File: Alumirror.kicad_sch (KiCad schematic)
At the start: 42 parts, among them J1 USB_C_Receptacle_USB2.0_16P_2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, J2 USB_C_Receptacle_USB2.0_16P_2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, J3 USB_C_Receptacle_USB2.0_16P_2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, J4 USB_C_Receptacle_USB2.0_16P_2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, SW1 BOOT, U1 CH552T, U2 CH552T, U3 USBLC6-2P6, U4 USBLC6-2P6, U5 USBLC6-2P6, U6 USBLC6-2P6

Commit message: Switch R14 back to 2010 size
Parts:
- R14: footprint Resistor_SMD:R_0805_2012Metric -> Resistor_SMD:R_2010_5025Metric
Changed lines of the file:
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@@
 			)
 		)
-		(property "Footprint" "Resistor_SMD:R_0805_2012Metric"
+		(property "Footprint" "Resistor_SMD:R_2010_5025Metric"
 			(at 128.27 62.738 90)
 			(effects

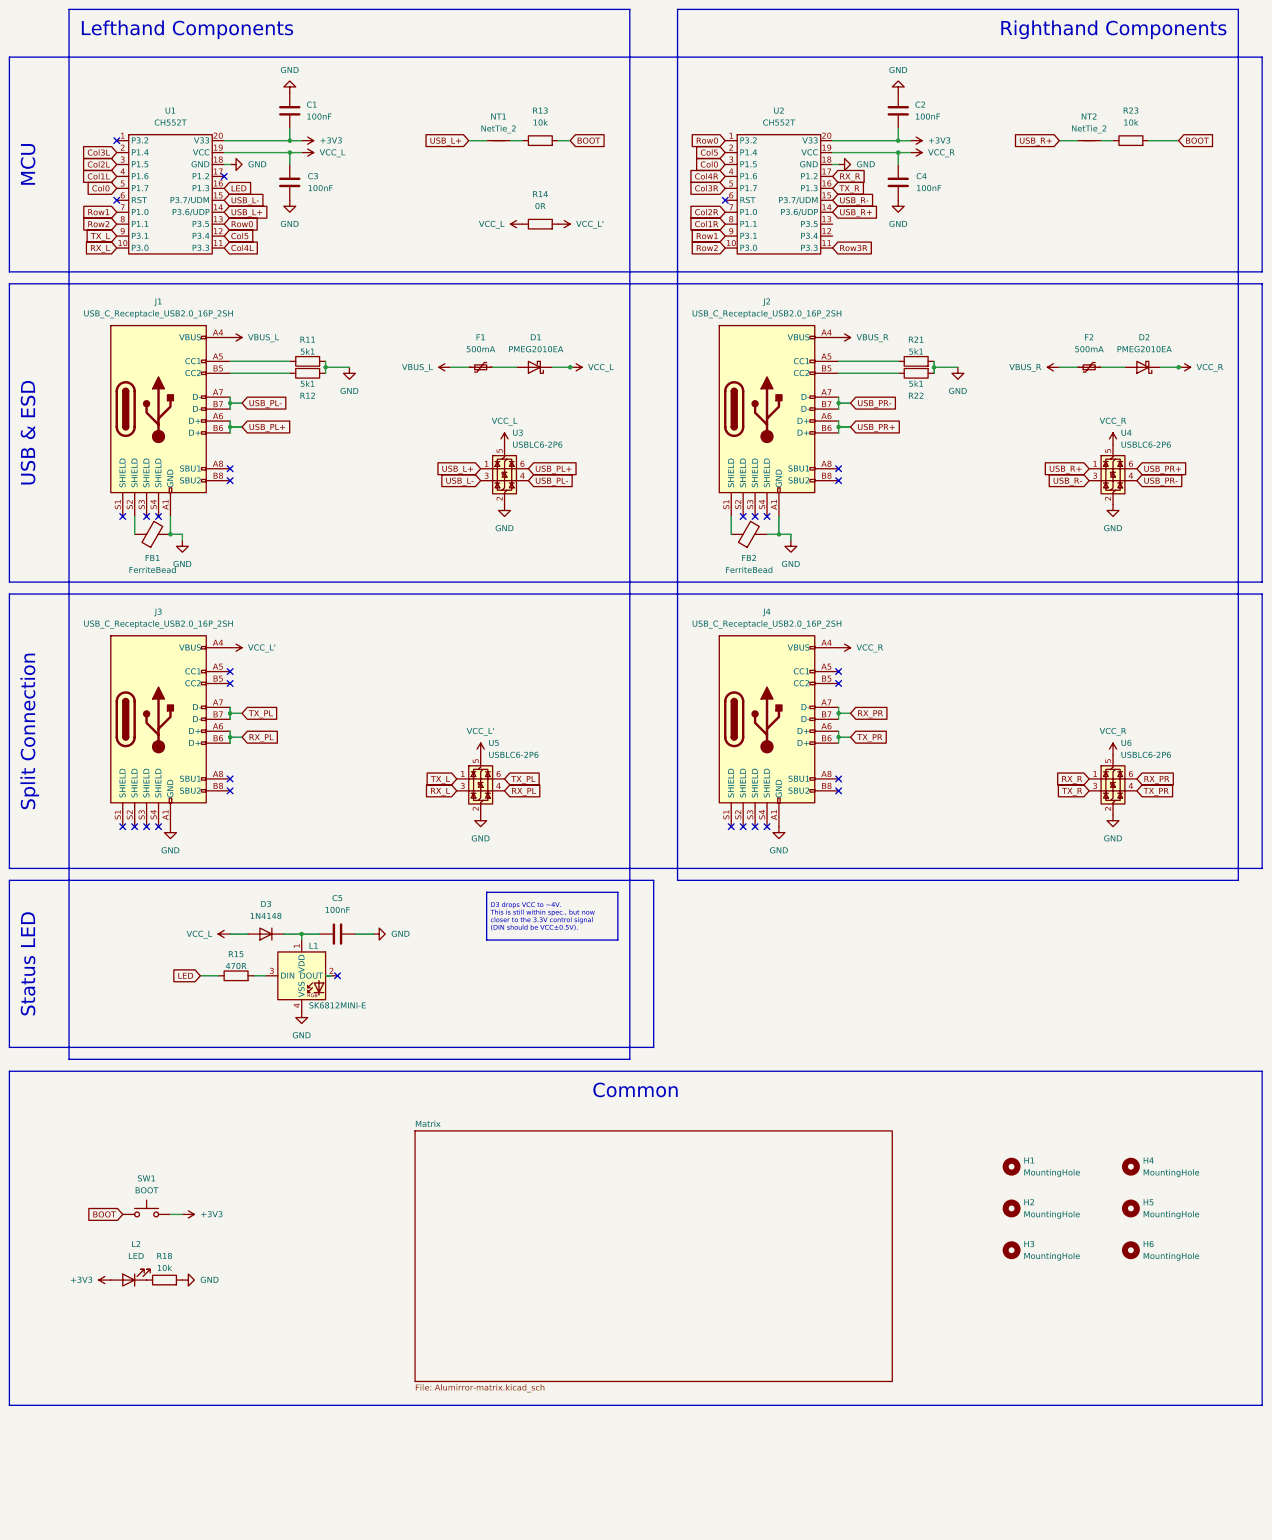
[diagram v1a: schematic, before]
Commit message: Shuffle components around again and fix DRC messages
 * Move split connection ESD chip to inside of associated USB port instead of above.
 * Scootch MCUs down.
 * Reduce clearance of ESD chip ground pin polygon pad.
 * Change solder nut hole to through-hole pad instead of NPT hole and solid pad.
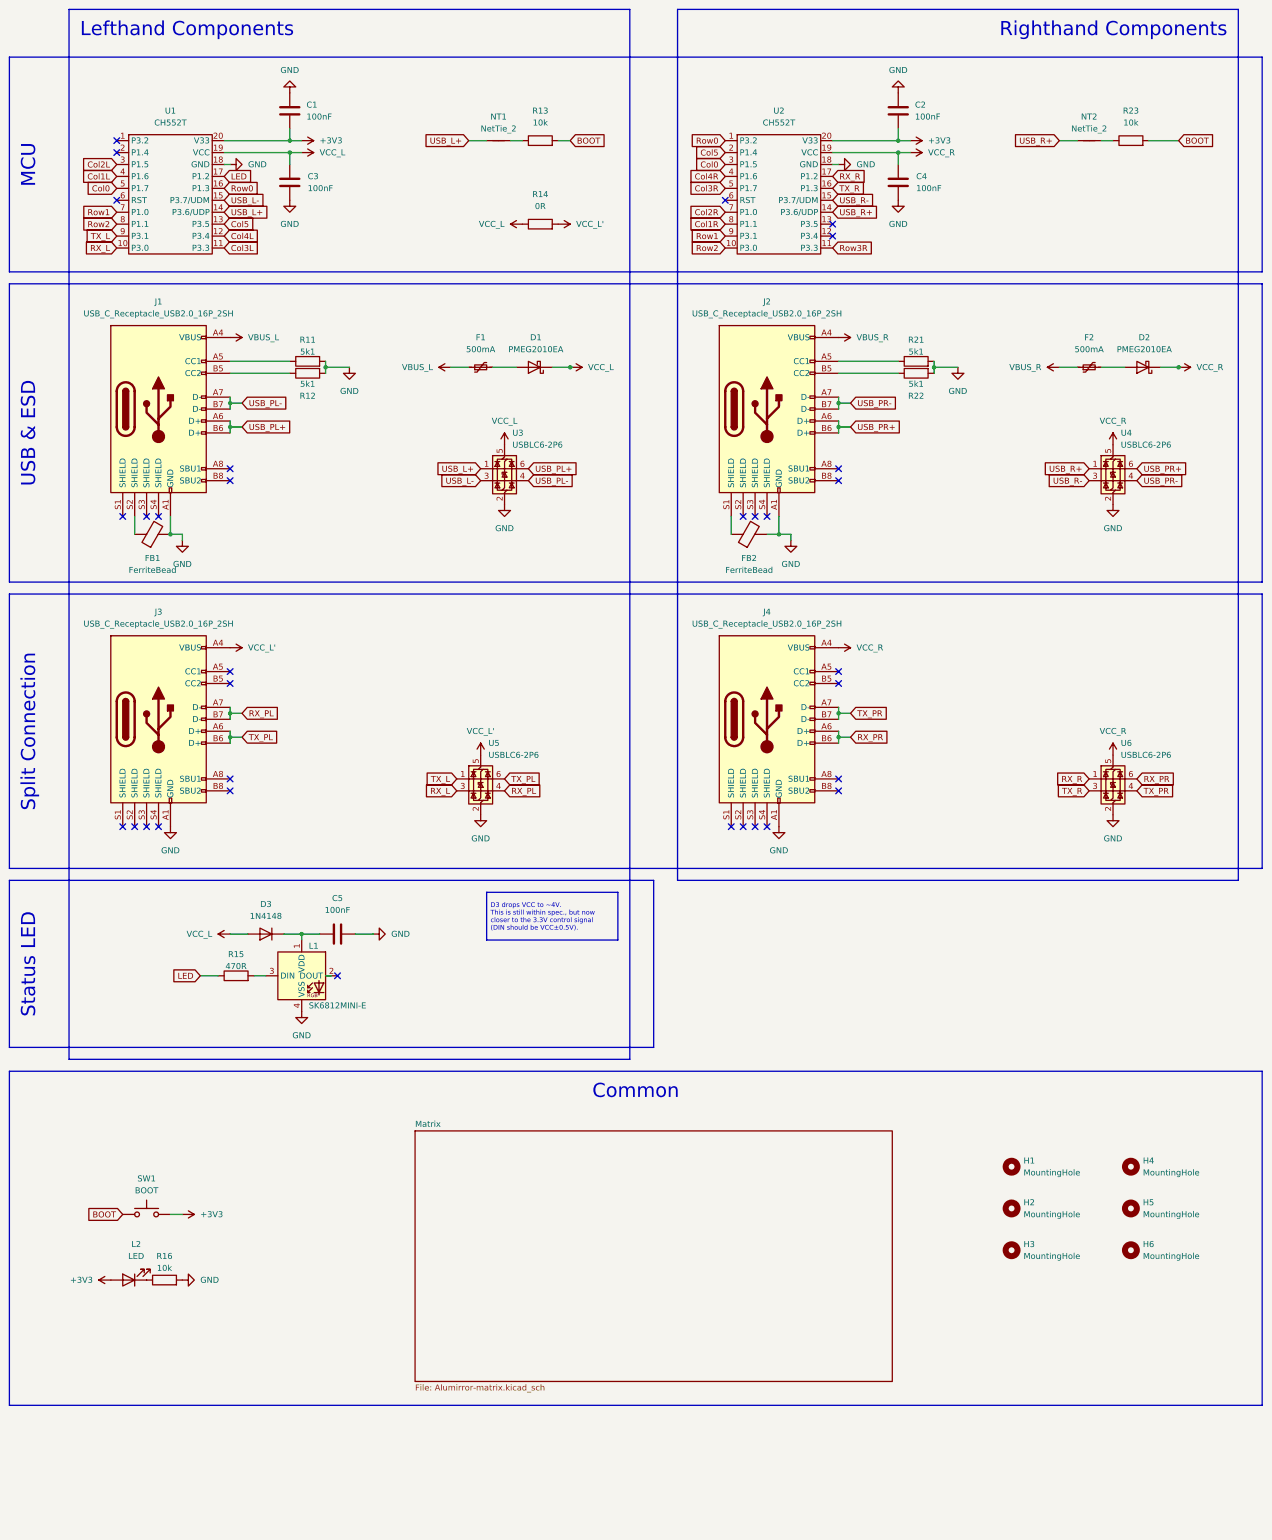
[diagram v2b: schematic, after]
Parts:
- renumbered R18 to R16
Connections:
- net Col3L: now also U1.11 (P3.3); no longer U1.2 (P1.4)
- net Col4L: now also U1.12 (P3.4); no longer U1.11 (P3.3)
- net Col5: now also U1.13 (P3.5); no longer U1.12 (P3.4)
- net LED: now also U1.17 (P1.2); no longer U1.16 (P1.3)
- net RX_PL: now also J3.A7 (D-), J3.B7 (D-); no longer J3.A6 (D+), J3.B6 (D+)
- net RX_PR: now also J4.A6 (D+), J4.B6 (D+); no longer J4.A7 (D-), J4.B7 (D-)
- net Row0: now also U1.16 (P1.3); no longer U1.13 (P3.5)
- net TX_PL: now also J3.A6 (D+), J3.B6 (D+); no longer J3.A7 (D-), J3.B7 (D-)
- net TX_PR: now also J4.A7 (D-), J4.B7 (D-); no longer J4.A6 (D+), J4.B6 (D+)
- no-connect marks 31 -> 33
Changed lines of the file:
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@@
 	)
 	(no_connect
+		(at 190.5 60.96)
+	)
+	(no_connect
 		(at 173.99 189.23)
 	)
@@
 	)
 	(no_connect
+		(at 190.5 63.5)
+	)
+	(no_connect
 		(at 85.09 220.98)
 	)
@@
 	)
 	(no_connect
-		(at 60.96 50.8)
+		(at 38.1 45.72)
 	)
 	(no_connect
@@
 	(global_label "Col4L"
 		(shape input)
-		(at 60.96 66.04 0)
+		(at 60.96 63.5 0)
 		(fields_autoplaced yes)
 		(effects
@@
 		)
 		(property "Intersheetrefs" "${INTERSHEET_REFS}"
-			(at 69.267 66.04 0)
+			(at 69.267 63.5 0)
 			(effects
 				(font
@@
 	(global_label "LED"
 		(shape input)
-		(at 60.96 53.34 0)
+		(at 60.96 50.8 0)
 		(fields_autoplaced yes)
 		(effects
@@
 		)
 		(property "Intersheetrefs" "${INTERSHEET_REFS}"
-			(at 67.3923 53.34 0)
+			(at 67.3923 50.8 0)
 			(effects
 				(font
@@
 	(global_label "RX_PL"
 		(shape input)
-		(at 64.77 170.18 0)
+		(at 64.77 165.1 0)
 		(fields_autoplaced yes)
 		(effects
@@
 		)
 		(property "Intersheetrefs" "${INTERSHEET_REFS}"
-			(at 73.5004 170.18 0)
+			(at 73.5004 165.1 0)
 			(effects
 				(font
@@
 	(global_label "Col3L"
 		(shape input)
-		(at 38.1 45.72 180)
+		(at 60.96 66.04 0)
 		(fields_autoplaced yes)
 		(effects
@@
 				(size 1.27 1.27)
 			)
-			(justify right)
+			(justify left)
 		)
 		(property "Intersheetrefs" "${INTERSHEET_REFS}"
-			(at 29.793 45.72 0)
+			(at 69.267 66.04 0)
 			(effects
 				(font
 					(size 1.27 1.27)
 				)
-				(justify right)
+				(justify left)
 				(hide yes)
 			)
@@
 	(global_label "Col5"
 		(shape input)
-		(at 60.96 63.5 0)
+		(at 60.96 60.96 0)
 		(fields_autoplaced yes)
 		(effects
@@
 		)
 		(property "Intersheetrefs" "${INTERSHEET_REFS}"
-			(at 68.2389 63.5 0)
+			(at 68.2389 60.96 0)
 			(effects
 				(font
@@
 	(global_label "TX_PL"
 		(shape input)
-		(at 64.77 165.1 0)
+		(at 64.77 170.18 0)
 		(fields_autoplaced yes)
 		(effects
@@
 		)
 		(property "Intersheetrefs" "${INTERSHEET_REFS}"
-			(at 73.198 165.1 0)
+			(at 73.198 170.18 0)
 			(effects
 				(font
@@
 	(global_label "RX_PR"
 		(shape input)
-		(at 194.31 165.1 0)
+		(at 194.31 170.18 0)
 		(fields_autoplaced yes)
 		(effects
@@
 		)
 		(property "Intersheetrefs" "${INTERSHEET_REFS}"
-			(at 203.2823 165.1 0)
+			(at 203.2823 170.18 0)
 			(effects
 				(font
@@
 	(global_label "TX_PR"
 		(shape input)
-		(at 194.31 170.18 0)
+		(at 194.31 165.1 0)
 		(fields_autoplaced yes)
 		(effects
@@
 		)
 		(property "Intersheetrefs" "${INTERSHEET_REFS}"
-			(at 202.9799 170.18 0)
+			(at 202.9799 165.1 0)
 			(effects
 				(font
@@
 	(global_label "Row0"
 		(shape input)
-		(at 60.96 60.96 0)
+		(at 60.96 53.34 0)
 		(fields_autoplaced yes)
 		(effects
@@
 		)
 		(property "Intersheetrefs" "${INTERSHEET_REFS}"
-			(at 68.9042 60.96 0)
+			(at 68.9042 53.34 0)
 			(effects
 				(font
@@
 		(on_board yes)
 		(dnp no)
-		(property "Reference" "R18"
+		(property "Reference" "R16"
 			(at 48.26 280.67 90)
 			(effects
@@
 			(project "Alumirror"
 				(path "/52f043ac-ccff-4c85-bc10-2db9d3c9e3f3"
-					(reference "R18")
+					(reference "R16")
 					(unit 1)
 				)

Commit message: Renumber components
 * For single-digit components:
   * Odd numbers are populated on the lefthand board only
   * Even numbers are populated on the righthand board only
 * Double-digit components are populated on both sides
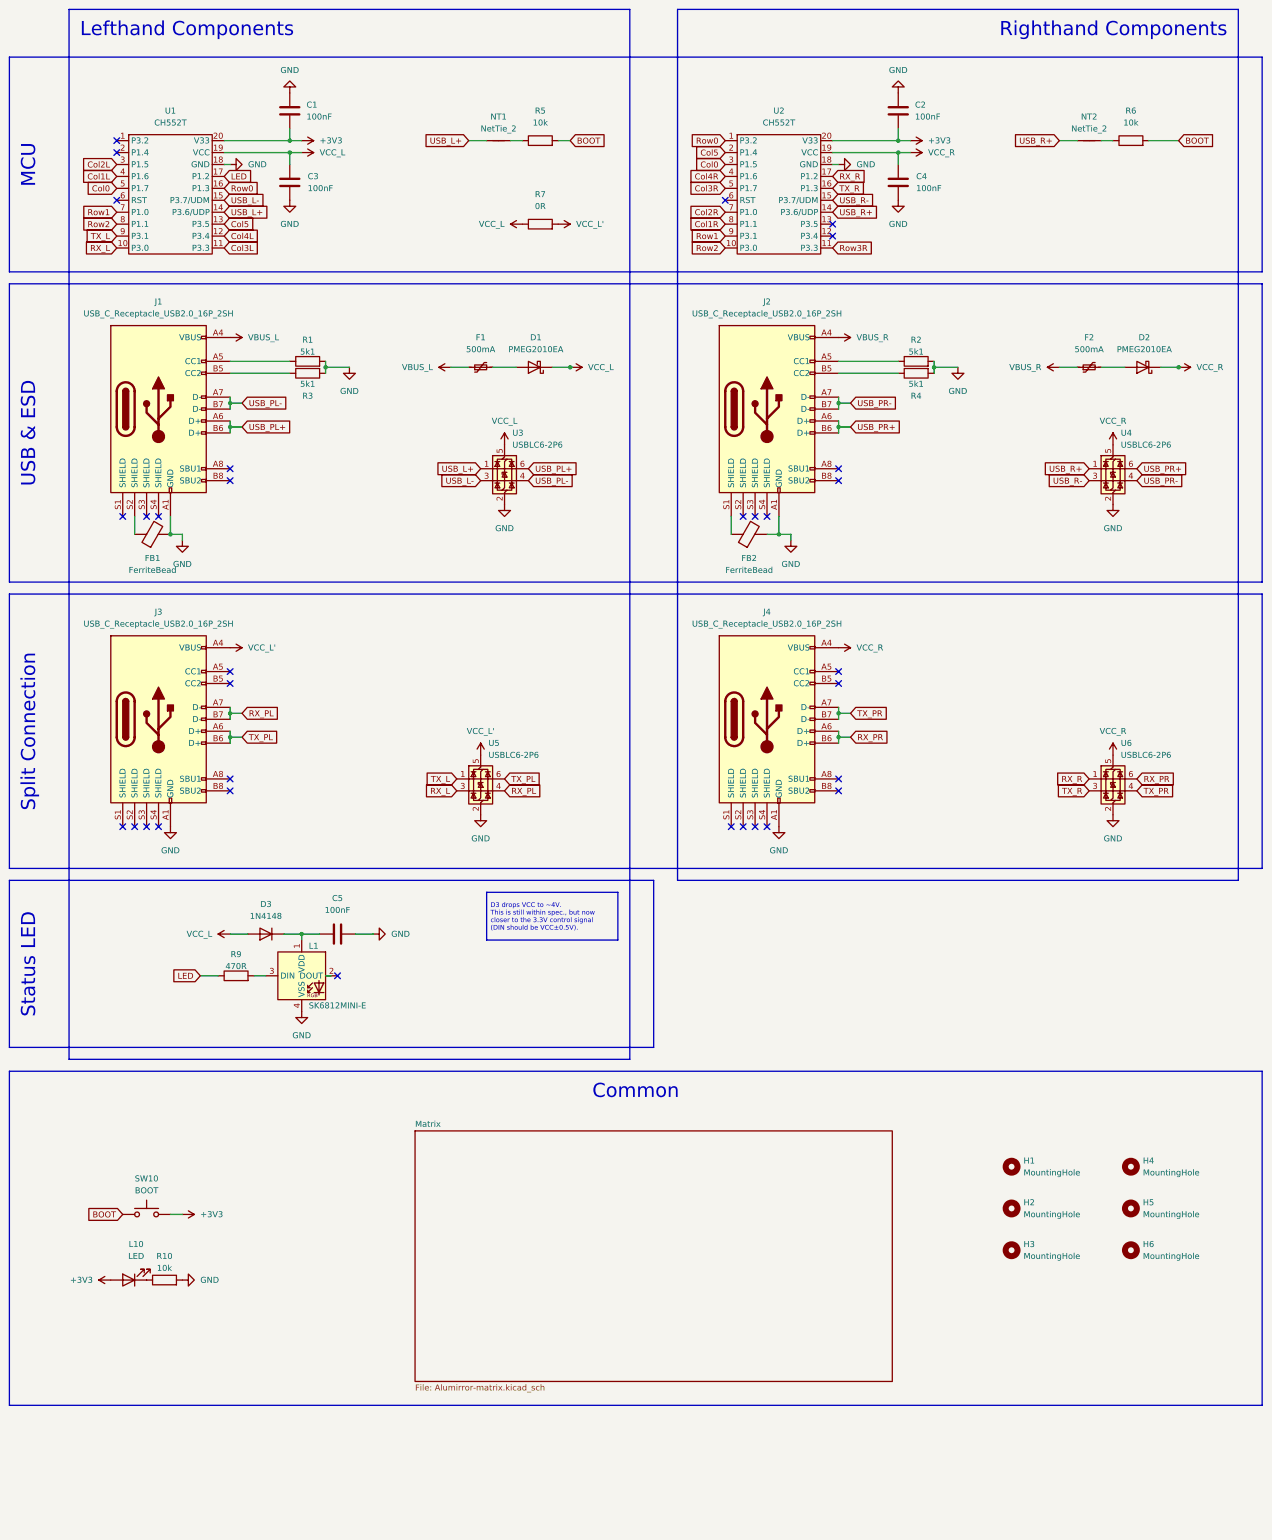
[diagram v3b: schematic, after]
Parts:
- renumbered L2 to L10, R11 to R1, R16 to R10, R21 to R2, R12 to R3, R22 to R4, R13 to R5, R23 to R6, R14 to R7, R15 to R9, SW1 to SW10
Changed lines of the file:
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@@
 		(dnp no)
 		(fields_autoplaced yes)
-		(property "Reference" "L2"
+		(property "Reference" "L10"
 			(at 42.2275 278.13 0)
 			(effects
@@
 			(project ""
 				(path "/52f043ac-ccff-4c85-bc10-2db9d3c9e3f3"
-					(reference "L2")
+					(reference "L10")
 					(unit 1)
 				)
@@
 		(on_board yes)
 		(dnp no)
-		(property "Reference" "R21"
+		(property "Reference" "R2"
 			(at 208.28 85.598 90)
 			(effects
@@
 			(project "Alumirror"
 				(path "/52f043ac-ccff-4c85-bc10-2db9d3c9e3f3"
-					(reference "R21")
+					(reference "R2")
 					(unit 1)
 				)
@@
 		(on_board yes)
 		(dnp no)
-		(property "Reference" "R11"
+		(property "Reference" "R1"
 			(at 78.74 85.598 90)
 			(effects
@@
 			(project "Alumirror"
 				(path "/52f043ac-ccff-4c85-bc10-2db9d3c9e3f3"
-					(reference "R11")
+					(reference "R1")
 					(unit 1)
 				)
@@
 		(dnp no)
 		(fields_autoplaced yes)
-		(property "Reference" "R13"
+		(property "Reference" "R5"
 			(at 128.27 36.83 90)
 			(effects
@@
 			(project "Alumirror"
 				(path "/52f043ac-ccff-4c85-bc10-2db9d3c9e3f3"
-					(reference "R13")
+					(reference "R5")
 					(unit 1)
 				)
@@
 		(on_board yes)
 		(dnp no)
-		(property "Reference" "R22"
+		(property "Reference" "R4"
 			(at 208.28 97.536 90)
 			(effects
@@
 			(project "Alumirror"
 				(path "/52f043ac-ccff-4c85-bc10-2db9d3c9e3f3"
-					(reference "R22")
+					(reference "R4")
 					(unit 1)
 				)
@@
 		(on_board yes)
 		(dnp no)
-		(property "Reference" "R15"
+		(property "Reference" "R9"
 			(at 63.5 216.408 90)
 			(effects
@@
 			(project "Alumirror"
 				(path "/52f043ac-ccff-4c85-bc10-2db9d3c9e3f3"
-					(reference "R15")
+					(reference "R9")
 					(unit 1)
 				)
@@
 		(dnp no)
 		(fields_autoplaced yes)
-		(property "Reference" "R23"
+		(property "Reference" "R6"
 			(at 254 36.83 90)
 			(effects
@@
 			(project "Alumirror"
 				(path "/52f043ac-ccff-4c85-bc10-2db9d3c9e3f3"
-					(reference "R23")
+					(reference "R6")
 					(unit 1)
 				)
@@
 		(on_board yes)
 		(dnp no)
-		(property "Reference" "R16"
+		(property "Reference" "R10"
 			(at 48.26 280.67 90)
 			(effects
@@
 			(project "Alumirror"
 				(path "/52f043ac-ccff-4c85-bc10-2db9d3c9e3f3"
-					(reference "R16")
+					(reference "R10")
 					(unit 1)
 				)
@@
 		(on_board yes)
 		(dnp no)
-		(property "Reference" "R12"
+		(property "Reference" "R3"
 			(at 78.74 97.536 90)
 			(effects
@@
 			(project "Alumirror"
 				(path "/52f043ac-ccff-4c85-bc10-2db9d3c9e3f3"
-					(reference "R12")
+					(reference "R3")
 					(unit 1)
 				)
@@
 		(dnp no)
 		(fields_autoplaced yes)
-		(property "Reference" "R14"
+		(property "Reference" "R7"
 			(at 128.27 54.61 90)
 			(effects
@@
 			(project "Alumirror"
 				(path "/52f043ac-ccff-4c85-bc10-2db9d3c9e3f3"
-					(reference "R14")
+					(reference "R7")
 					(unit 1)
 				)
@@
 		(dnp no)
 		(fields_autoplaced yes)
-		(property "Reference" "SW1"
+		(property "Reference" "SW10"
 			(at 44.45 264.16 0)
 			(effects
@@
 			(project "Alumirror"
 				(path "/52f043ac-ccff-4c85-bc10-2db9d3c9e3f3"
-					(reference "SW1")
+					(reference "SW10")
 					(unit 1)
 				)
